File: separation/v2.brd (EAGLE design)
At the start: 6 parts

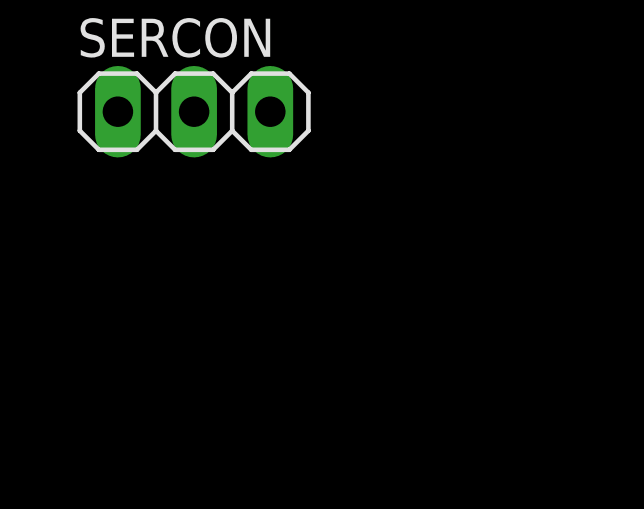
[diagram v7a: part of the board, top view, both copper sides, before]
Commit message: add potential divider
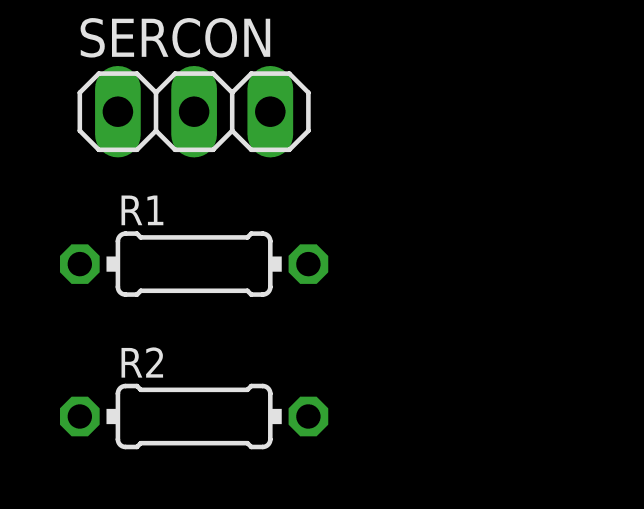
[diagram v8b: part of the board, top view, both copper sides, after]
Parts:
- added R1: 220k, rcl:0204/7
- added R2: 120k, rcl:0204/7
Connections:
- new net VSENSE: R1.2, R2.1
- net GND: now also R2.2
- net VBAT: now also R1.1
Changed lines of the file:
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@@
 <attribute name="VALUE" x="-50.8" y="-61.595" size="1.27" layer="27"/>
+</element>
+<element name="R1" library="rcl" library_urn="urn:adsk.eagle:library:334" package="0204/7" package3d_urn="urn:adsk.eagle:package:23498/2" value="220k" x="-46.99" y="-63.5" smashed="yes">
+<attribute name="NAME" x="-49.53" y="-62.2046" size="0.9906" layer="25" ratio="10"/>
+<attribute name="POPULARITY" value="79" x="-46.99" y="-63.5" size="1.778" layer="27" font="vector" ratio="15" display="off"/>
+<attribute name="SPICEPREFIX" value="R" x="-46.99" y="-63.5" size="1.778" layer="27" font="vector" ratio="15" display="off"/>
+<attribute name="VALUE" x="-48.6156" y="-63.9826" size="0.9906" layer="27" ratio="10"/>
+</element>
+<element name="R2" library="rcl" library_urn="urn:adsk.eagle:library:334" package="0204/7" package3d_urn="urn:adsk.eagle:package:23498/2" value="120k" x="-46.99" y="-68.58" smashed="yes">
+<attribute name="NAME" x="-49.53" y="-67.2846" size="0.9906" layer="25" ratio="10"/>
+<attribute name="POPULARITY" value="79" x="-46.99" y="-68.58" size="1.778" layer="27" font="vector" ratio="15" display="off"/>
+<attribute name="SPICEPREFIX" value="R" x="-46.99" y="-68.58" size="1.778" layer="27" font="vector" ratio="15" display="off"/>
+<attribute name="VALUE" x="-48.6156" y="-69.0626" size="0.9906" layer="27" ratio="10"/>
 </element>
 </elements>
@@
 <contactref element="LDO" pad="2"/>
 <contactref element="LOUD" pad="2"/>
+<contactref element="R2" pad="2"/>
+<wire x1="-46.99" y1="-58.42" x2="-43.18" y2="-68.58" width="0" layer="19" extent="1-1"/>
 <wire x1="-42.22" y1="-48.26" x2="-46.99" y2="-58.42" width="0" layer="19" extent="1-1"/>
 <wire x1="-31.74" y1="-52.07" x2="-42.22" y2="-48.26" width="0" layer="19" extent="1-1"/>
@@
 <contactref element="BAT" pad="1"/>
 <contactref element="LDO" pad="1"/>
+<contactref element="R1" pad="1"/>
+<wire x1="-49.53" y1="-58.42" x2="-50.8" y2="-63.5" width="0" layer="19" extent="1-1"/>
 <wire x1="-45.72" y1="-48.26" x2="-49.53" y2="-58.42" width="0" layer="19" extent="1-1"/>
 <wire x1="-34.29" y1="-52.07" x2="-45.72" y2="-48.26" width="0" layer="19" extent="1-1"/>
@@
 <contactref element="LOUD" pad="1"/>
 </signal>
+<signal name="VSENSE">
+<contactref element="R1" pad="2"/>
+<contactref element="R2" pad="1"/>
+<wire x1="-43.18" y1="-63.5" x2="-50.8" y2="-68.58" width="0" layer="19" extent="1-1"/>
+</signal>
 </signals>
